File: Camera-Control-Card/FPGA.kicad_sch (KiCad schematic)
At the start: 63 parts, among them U1 LCMXO2-7000HC-6TG144I, U11 T602-025.0M

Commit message: test
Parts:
- removed TP10, TP11, TP12, TP13, TP14, TP15, TP7, TP8, TP9: TestPoint, TestPoint:TestPoint_Pad_1.0x1.0mm, symbol Connector:TestPoint
- added D6, D7, D8, D9: B, Resistor_SMD:R_0603_1608Metric, symbol Device:LED
- added R25, R26, R27, R28: 1K, Resistor_SMD:R_0603_1608Metric, symbol Device:R
- C1, C2: footprint Capacitor_SMD:C_0805_2012Metric -> Capacitor_SMD:C_0603_1608Metric
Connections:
- net +3V3: no longer C57.1, C58.1
- net GND: now also C57.1, C58.1, D6.1 (K), D7.1 (K), D8.1 (K), D9.1 (K)
- new net: D9.2 (A), R28.1
- new net: D7.2 (A), R26.1
- new net: D8.2 (A), R27.1
- new net: D6.2 (A), R25.1
- new net LED_0: R25.2
- new net LED_1: R26.2
- new net LED_2: R27.2
- new net LED_3: R28.2
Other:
- note removed: "Pullups"
- moved on the sheet: C1, C2, C28, C29, C30, C31, C32, C33, C34, C35, C36, C37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

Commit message: Updates
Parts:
- added D16: B, LED_SMD:LED_0603_1608Metric, symbol Device:LED
- added R37: 1K, Resistor_SMD:R_0603_1608Metric, symbol Device:R
- D1: renamed from D6; footprint Resistor_SMD:R_0603_1608Metric -> LED_SMD:LED_0603_1608Metric
- D2: renamed from D7; footprint Resistor_SMD:R_0603_1608Metric -> LED_SMD:LED_0603_1608Metric
- D3: renamed from D8; footprint Resistor_SMD:R_0603_1608Metric -> LED_SMD:LED_0603_1608Metric
- D4: renamed from D9; footprint Resistor_SMD:R_0603_1608Metric -> LED_SMD:LED_0603_1608Metric
- R1: renamed from R4; footprint Resistor_SMD:R_0805_2012Metric -> Resistor_SMD:R_0603_1608Metric
- R10: renamed from R7; footprint Resistor_SMD:R_0805_2012Metric -> Resistor_SMD:R_0603_1608Metric
- R11: renamed from R8; footprint Resistor_SMD:R_0805_2012Metric -> Resistor_SMD:R_0603_1608Metric
- R12: renamed from R11; footprint Resistor_SMD:R_0805_2012Metric -> Resistor_SMD:R_0603_1608Metric
- R2: renamed from R1; footprint Resistor_SMD:R_0805_2012Metric -> Resistor_SMD:R_0603_1608Metric
- R3: renamed from R2; footprint Resistor_SMD:R_0805_2012Metric -> Resistor_SMD:R_0603_1608Metric
- R4: renamed from R3; footprint Resistor_SMD:R_0805_2012Metric -> Resistor_SMD:R_0603_1608Metric
- R5: renamed from R9; footprint Resistor_SMD:R_0805_2012Metric -> Resistor_SMD:R_0603_1608Metric
- R6: renamed from R10; footprint Resistor_SMD:R_0805_2012Metric -> Resistor_SMD:R_0603_1608Metric
- R7: renamed from R12; footprint Resistor_SMD:R_0805_2012Metric -> Resistor_SMD:R_0603_1608Metric
- R8: renamed from R5; footprint Resistor_SMD:R_0805_2012Metric -> Resistor_SMD:R_0603_1608Metric
- R9: renamed from R6; footprint Resistor_SMD:R_0805_2012Metric -> Resistor_SMD:R_0603_1608Metric
- renumbered C33 to C10, C40 to C11, C41 to C12, C35 to C13, C36 to C14, C38 to C15, C42 to C16, C34 to C17, C37 to C18, C39 to C19, C43 to C20, C45 to C21, C52 to C22, C46 to C23, C48 to C24, C50 to C25, C53 to C26, C47 to C27, C49 to C28, C51 to C29, C54 to C30, C1 to C31, C2 to C32, C61 to C33, C55 to C34, C57 to C35, C59 to C36, C62 to C37, C56 to C38, C58 to C39, C28 to C4, C60 to C40, C63 to C41, C30 to C5, C32 to C6, C44 to C7, C29 to C8, C31 to C9, R25 to R13, R26 to R14, R27 to R15, R28 to R16, TP19 to TP1, U11 to U2
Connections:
- net GND: now also D16.1 (K)
- net OSC_OUT: no longer U1.128 (PT18A)
- net PT35B: now reaches U1.111 (PT35B)
- net PT35A: now reaches U1.112 (PT35A)
- net PT33B: now reaches U1.113 (PT33B)
- net PT33A: now reaches U1.114 (PT33A)
- net PT28B: now reaches U1.115 (PT28B)
- net PT28A: now reaches U1.117 (PT28A)
- net PT25B: now reaches U1.121 (PT25B)
- net PT25A: now reaches U1.122 (PT25A)
- net PT18B: now reaches U1.127 (PT18B)
- net SCL renamed PT22C
- net SDA renamed PT22D
- new net: D16.2 (A), R37.1
- new net LED_4: R37.2
- new net PT18A: U1.128 (PT18A)
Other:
- moved on the sheet: D1, D2, D3, D4, R13, R14, R15, R16

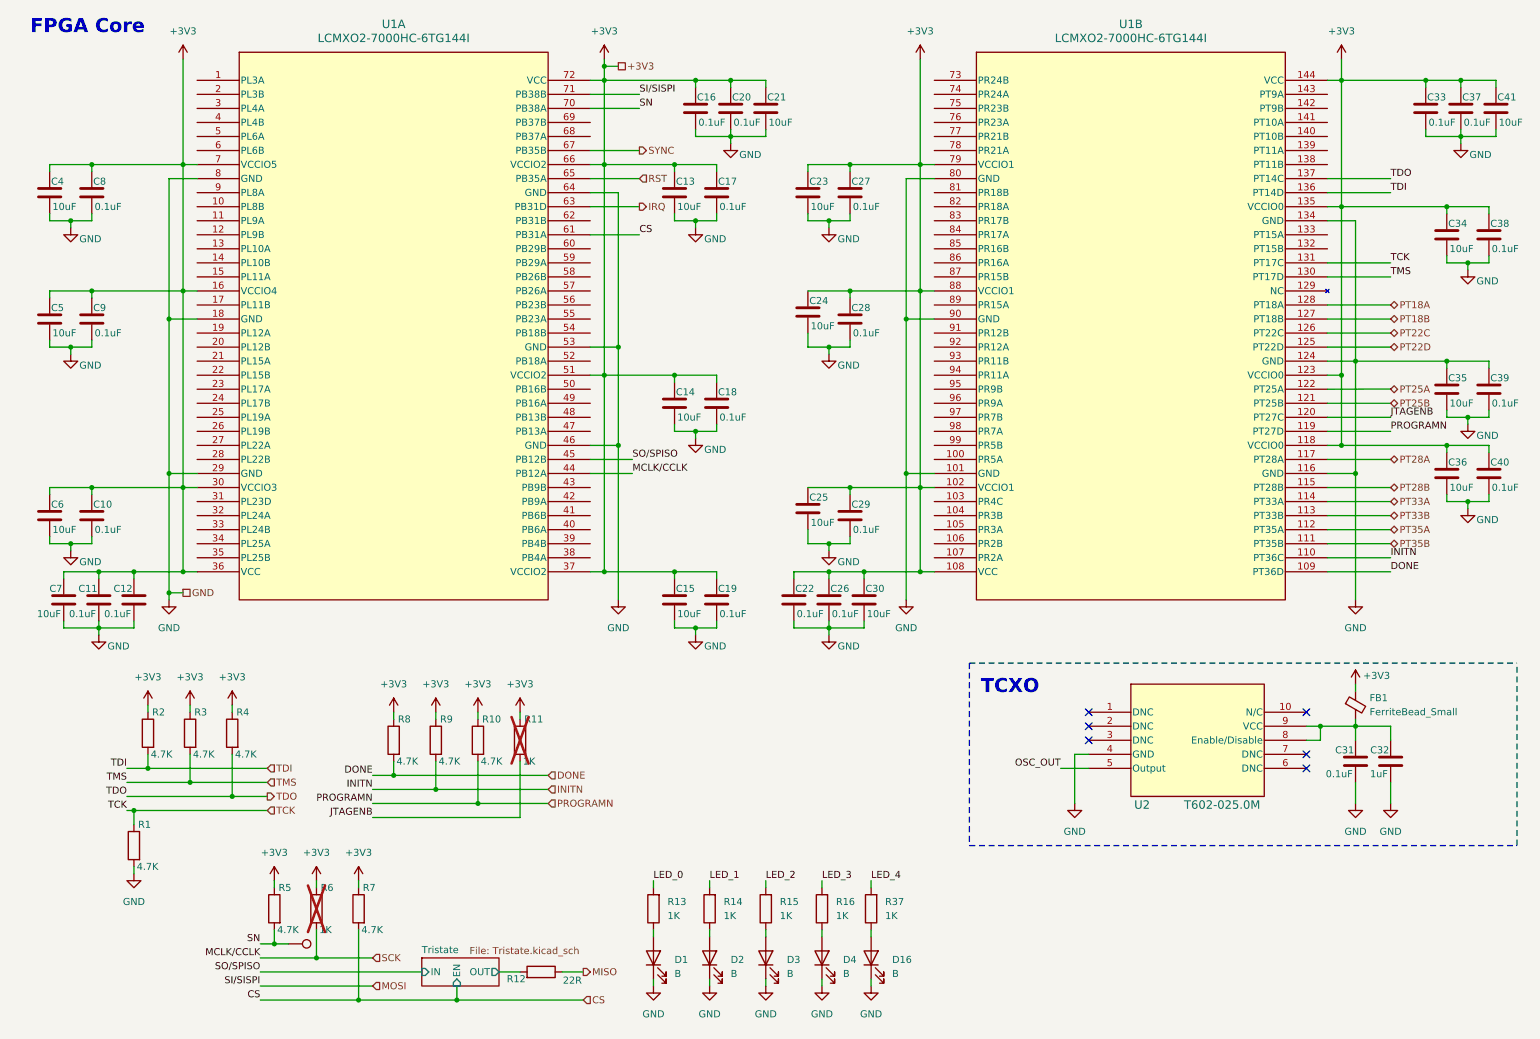
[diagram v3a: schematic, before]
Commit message: Camera Control Card layout
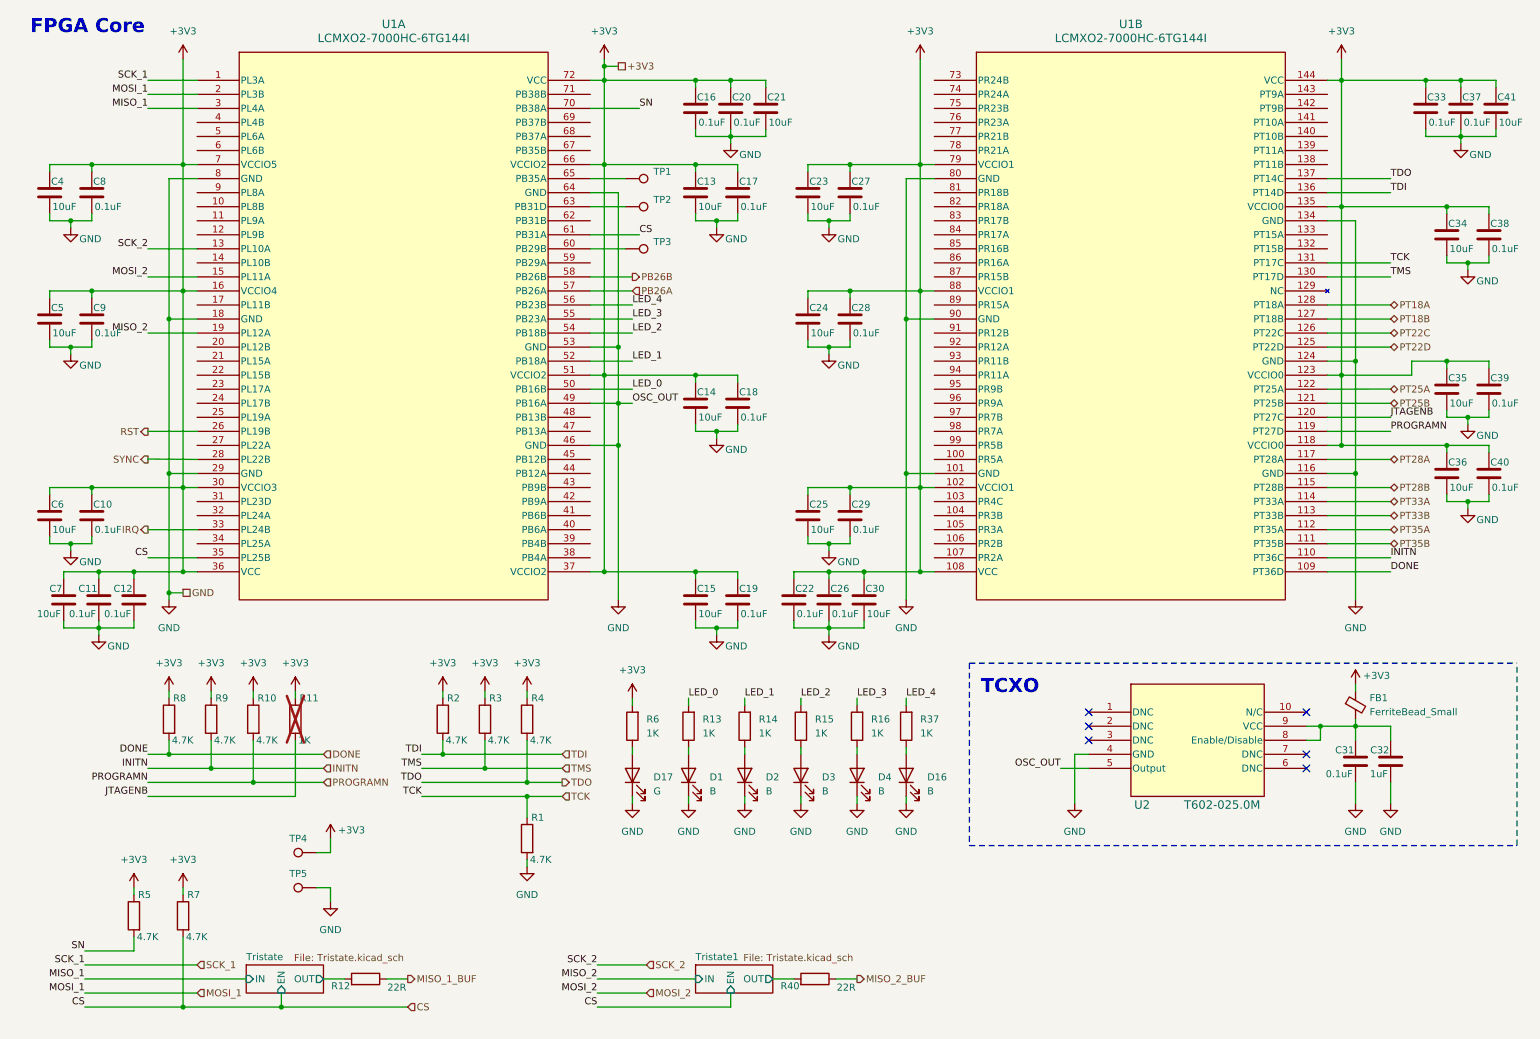
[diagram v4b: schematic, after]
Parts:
- added D17: G, LED_SMD:LED_0603_1608Metric, symbol Device:LED
- added R40: 22R, Resistor_SMD:R_0603_1608Metric, symbol Device:R
- added TP2, TP3, TP4, TP5: TestPoint, TestPoint:TestPoint_Pad_D1.0mm, symbol Connector:TestPoint
- R6: now fitted
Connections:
- net OSC_OUT is gone; now on net GND: U2.5 (Output)
- net +3V3: now also C35.1, C39.1, R6.2, TP4.1; no longer R6.1
- net CS: now also U1.35 (PL25B)
- net GND: now also U1.49 (PB16A), D17.1 (K), TP5.1; no longer C35.1, C39.1
- net IRQ: now also U1.33 (PL24B); no longer U1.63 (PB31D)
- net LED_0: now also U1.50 (PB16B)
- net LED_1: now also U1.52 (PB18A)
- net LED_2: now also U1.54 (PB18B)
- net LED_3: now also U1.55 (PB23A)
- net LED_4: now also U1.56 (PB23B)
- net RST: now also U1.26 (PL19B); no longer U1.65 (PB35A)
- net SN: no longer TP1.1
- net SYNC: now also U1.28 (PL22B); no longer U1.67 (PB35B)
- net SCK_1: now reaches U1.1 (PL3A)
- net SCK_2: now reaches U1.13 (PL10A)
- net MOSI_2: now reaches U1.15 (PL11A)
- net MISO_2: now reaches U1.19 (PL12A)
- net MOSI_1: now reaches U1.2 (PL3B)
- net MISO_1: now reaches U1.3 (PL4A)
- net PB26A: now reaches U1.57 (PB26A)
- net PB26B: now reaches U1.58 (PB26B)
- net at U1.60 (PB29B): now also TP3.1
- net MISO renamed MISO_1_BUF
- net MOSI: no longer names the net of U1.71 (PB38B)
- net SCK: no longer names the net of U1.44 (PB12A)
- net SCK: no longer R6.2
- net SO/SPISO: no longer names the net of U1.45 (PB12B)
- new net: TP2.1, U1.63 (PB31D)
- new net: D17.2 (A), R6.1
- new net: TP1.1, U1.65 (PB35A)
- new net MISO_2_BUF: R40.1
- new net Tristate1/OUT: R40.2
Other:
- added sheet Tristate1 (Tristate.kicad_sch)
- moved on the sheet: C13, C14, C15, C17, C18, C19, C24, C25, D1, D16, D2, D3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

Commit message: Layout completed for camera control card
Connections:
- net CS: no longer U1.61 (PB31A)
- net PR5A: now reaches U1.100 (PR5A)
- net PR4C: now reaches U1.103 (PR4C)
- net PR3B: now reaches U1.104 (PR3B)
- net PR3A: now reaches U1.105 (PR3A)
- net PR2B: now reaches U1.106 (PR2B)
- net PR24B: now reaches U1.73 (PR24B)
- net PR24A: now reaches U1.74 (PR24A)
- net PR23B: now reaches U1.75 (PR23B)
- net PR23A: now reaches U1.76 (PR23A)
- net PR5B: now reaches U1.99 (PR5B)
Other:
- moved on the sheet: C25, C29
